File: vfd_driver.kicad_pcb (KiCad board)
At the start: 2 copper layers, 35 parts, among them CON1 AVR-ISP-6, J1 Conn_01x02, J2 futaba_7_lt_44z, J3 Input, Q1 IRLZ34, Q2 60N03L, Q3 BC817, Q4 BC807, Q5 BC817, Q6 BC807, T1 Transformer_1P_SS, U1 ATTINY13-20PU, U2 74HC595, U3 74HC595, U4 74HC595, U5 TBD62783A, U6 TBD62783A, U7 TBD62783A

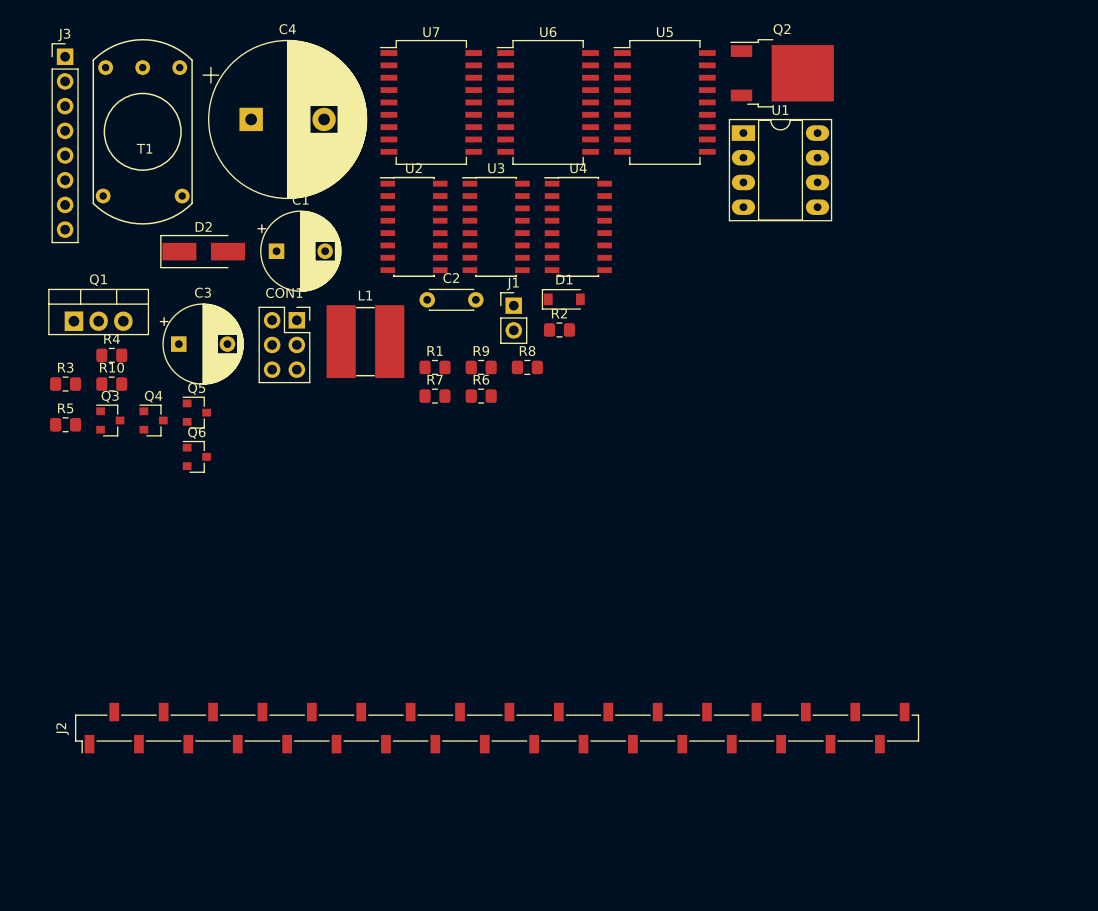
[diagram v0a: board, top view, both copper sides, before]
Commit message: add the datasheet of the vfd display
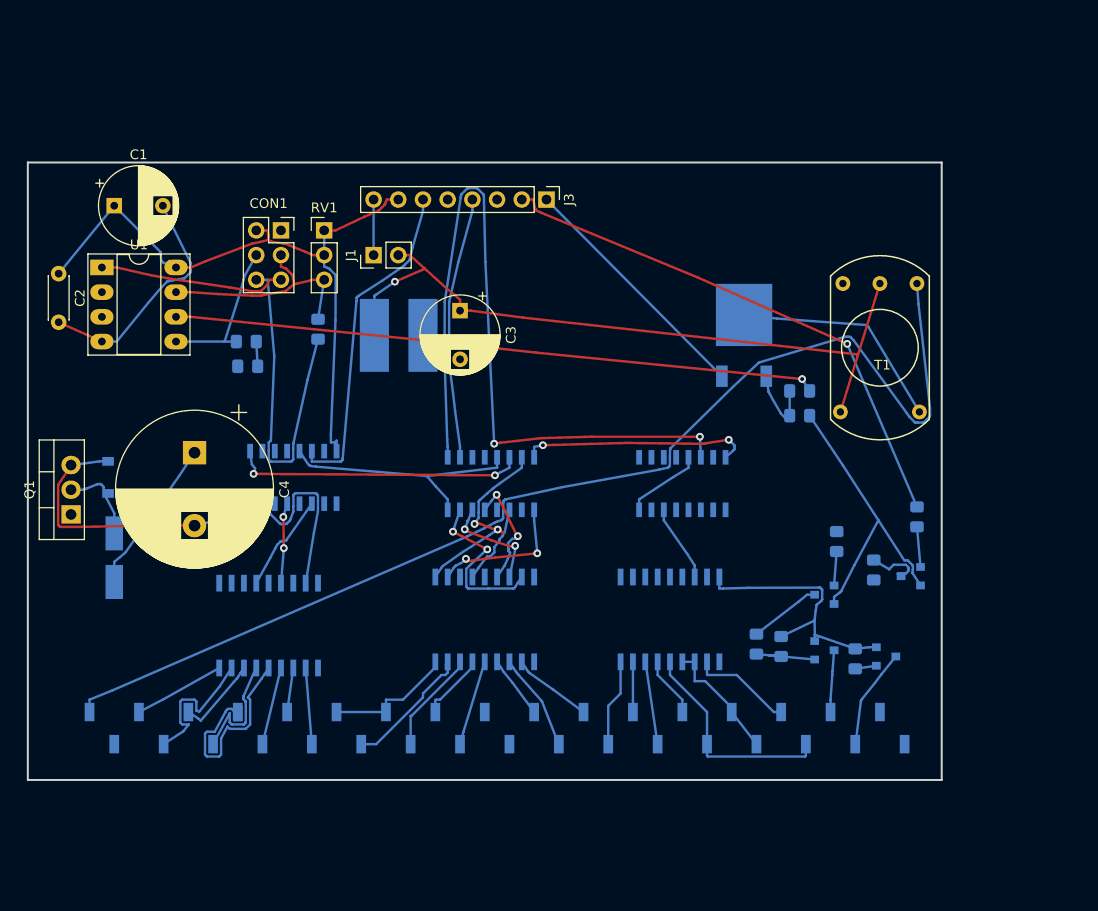
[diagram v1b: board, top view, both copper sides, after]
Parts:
- added R11: 1K, Resistor_SMD:R_0805_2012Metric_Pad1.15x1.40mm_HandSolder, B.Cu at (45.1, 29.8)
- added RV1: 10k, Connector_PinHeader_2.54mm:PinHeader_1x03_P2.54mm_Vertical, F.Cu at (45.7, 19.7)
- D1, D2, J2, L1, Q2, Q3, Q4, Q5, Q6, R1, R10, R2, R3, R4, R5, R6, R7, R8, R9, U2, U3, U4, U5, U6, U7: moved to B.Cu
- T1: footprint custom:Transformer_toroid_v_10mm -> modules:Transformer_toroid_v_10mm
- moved R5 88.1 mm to (106.7, 49.1), turned to 270 degrees
- moved Q3 83.9 mm to (106.0, 55.2), turned to 180 degrees
- moved Q4 79.1 mm to (103.5, 63.5)
- moved T1 79.0 mm to (102.9, 31.8)
- moved R3 75.5 mm to (94.6, 36.2)
- moved R10 71.5 mm to (90.2, 62.2), turned to 270 degrees
- moved R4 71.0 mm to (94.6, 38.7)
- moved Q6 67.5 mm to (97.2, 62.9)
- moved U5 67.5 mm to (40.0, 60.3), turned to 270 degrees
- moved U1 67.4 mm to (22.9, 23.5)
- moved Q5 67.2 mm to (97.2, 57.1), turned to 180 degrees
- moved U7 58.6 mm to (81.3, 59.7), turned to 270 degrees
- moved U6 53.6 mm to (62.2, 59.7), turned to 270 degrees
- moved J3 51.6 mm to (68.6, 16.5), turned to 270 degrees
- moved D1 50.4 mm to (23.5, 45.1), turned to 90 degrees
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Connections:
- net /SCK renamed /ADC
- J2 pad 17: (no net) -> Net-(J2-Pad17)
- J2 pad 18: (no net) -> Net-(J2-Pad18)
- J2 pad 2: (no net) -> Net-(J2-Pad2)
- J2 pad 33: (no net) -> Net-(J2-Pad33)
- U1 pad 2: (no net) -> Net-(U1-Pad2)
- U1 pad 3: (no net) -> Net-(U1-Pad3)
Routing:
- net GND: track 0.00 -> 182.6 mm
- net /FIL_n: track 0.00 -> 117.9 mm
- net VCC: track 0.00 -> 93.2 mm, vias 0 -> 2
- net /Q1: track 0.00 -> 79.0 mm, vias 0 -> 2
- net /5VOLT: track 0.00 -> 74.2 mm, vias 0 -> 1
- net /FILAMENT: track 0.00 -> 66.2 mm, vias 0 -> 1
- net /GRAD: track 0.00 -> 55.4 mm, vias 0 -> 1
- net +36V: track 0.00 -> 43.8 mm
- net /DATA: track 0.00 -> 34.1 mm
- net /Q0: track 0.00 -> 30.1 mm, vias 0 -> 2
- net /nSRCLR: track 0.00 -> 26.9 mm
- net /S6: track 0.00 -> 24.4 mm
- net /ADC: track 0.00 -> 23.3 mm
- net Net-(Q2-Pad2): track 0.00 -> 23.1 mm
- net /G1: track 0.00 -> 22.7 mm
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- added copper zone on B.Cu, net GND
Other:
- board outline added: 94 x 63.5 mm
- net class power added: clearance 0.2, trace_width 0.508, via_dia 0.8, via_drill 0.4
- net class signal added: clearance 0.2, trace_width 0.4064, via_dia 0.8, via_drill 0.4

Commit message: working on layout
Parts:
- added R12: 0, Resistor_SMD:R_1206_3216Metric, B.Cu at (31.0, 40.6)
- moved L1 33.9 mm to (23.4, 46.3), turned to 270 degrees
- moved R11 23.9 mm to (21.7, 34.7), turned to 0 degrees
- moved C4 17.8 mm to (31.2, 60.3), turned to 90 degrees
- moved J1 11.5 mm to (43.2, 30.9), turned to 0 degrees
- moved D1 11.1 mm to (17.8, 54.6)
- moved D2 10.7 mm to (21.2, 63.6), turned to 180 degrees
- moved Q1 9.44 mm to (20.6, 58.3)
- moved RV1 9.16 mm to (36.6, 20.2)
- moved R2 8.75 mm to (30.0, 37.5)
- moved R1 8.57 mm to (30.0, 34.8)
- moved C3 6.50 mm to (53.2, 28.4), turned to 180 degrees
- moved CON1 5.34 mm to (41.5, 25.0), turned to 180 degrees
- moved U2 1.20 mm to (41.5, 45.7)
- moved U5 1.14 mm to (40.0, 59.2)
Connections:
- C3 pad 1: /5VOLT -> +5V
- J3 pad 3: /RCLK -> /DATA
- J3 pad 4: /nSRCLR -> /RCLK
- J3 pad 6: /DATA -> /nSRCLR
- L1 pad 1: /5VOLT -> Net-(L1-Pad1)
- U2 pad 1: Net-(U2-Pad1) -> /Q1B
- U2 pad 15: Net-(U2-Pad15) -> /Q1A
- U2 pad 2: Net-(U2-Pad2) -> /Q1C
- U2 pad 3: Net-(U2-Pad3) -> /Q1D
- U2 pad 4: Net-(U2-Pad4) -> /Q1E
- U2 pad 5: Net-(U2-Pad5) -> /Q1F
- U2 pad 6: Net-(U2-Pad6) -> /Q1G
- U2 pad 7: Net-(U2-Pad7) -> /Q1H
- U3 pad 1: Net-(U3-Pad1) -> /Q2B
- U3 pad 15: Net-(U3-Pad15) -> /Q2A
- U3 pad 2: Net-(U3-Pad2) -> /Q2C
- U3 pad 3: Net-(U3-Pad3) -> /Q2D
- U3 pad 4: Net-(U3-Pad4) -> /Q2E
- U3 pad 5: Net-(U3-Pad5) -> /Q2F
- U3 pad 6: Net-(U3-Pad6) -> /Q2G
- U3 pad 7: Net-(U3-Pad7) -> /Q2H
- U4 pad 1: Net-(U4-Pad1) -> /Q3B
- U4 pad 15: Net-(U4-Pad15) -> /Q3A
- U4 pad 2: Net-(U4-Pad2) -> /Q3C
- U4 pad 3: Net-(U4-Pad3) -> /Q3D
- U4 pad 4: Net-(U4-Pad4) -> /Q3E
- U4 pad 5: Net-(U4-Pad5) -> /Q3F
- U4 pad 6: Net-(U4-Pad6) -> /Q3G
- U4 pad 7: Net-(U4-Pad7) -> /Q3H
- U5 pad 1: Net-(U2-Pad15) -> /Q1H
- U5 pad 2: Net-(U2-Pad1) -> /Q1G
- U5 pad 3: Net-(U2-Pad2) -> /Q1F
- U5 pad 4: Net-(U2-Pad3) -> /Q1E
- U5 pad 5: Net-(U2-Pad4) -> /Q1D
- U5 pad 6: Net-(U2-Pad5) -> /Q1C
- U5 pad 7: Net-(U2-Pad6) -> /Q1B
- U5 pad 8: Net-(U2-Pad7) -> /Q1A
- U6 pad 1: Net-(U3-Pad15) -> /Q2H
- U6 pad 2: Net-(U3-Pad1) -> /Q2G
- U6 pad 3: Net-(U3-Pad2) -> /Q2F
- U6 pad 4: Net-(U3-Pad3) -> /Q2E
- U6 pad 5: Net-(U3-Pad4) -> /Q2D
- U6 pad 6: Net-(U3-Pad5) -> /Q2C
- U6 pad 7: Net-(U3-Pad6) -> /Q2B
- U6 pad 8: Net-(U3-Pad7) -> /Q2A
- U7 pad 1: Net-(U4-Pad15) -> /Q3H
- U7 pad 2: Net-(U4-Pad1) -> /Q3G
- U7 pad 3: Net-(U4-Pad2) -> /Q3F
- U7 pad 4: Net-(U4-Pad3) -> /Q3E
- U7 pad 5: Net-(U4-Pad4) -> /Q3D
- U7 pad 6: Net-(U4-Pad5) -> /Q3C
- U7 pad 7: Net-(U4-Pad6) -> /Q3B
- U7 pad 8: Net-(U4-Pad7) -> /Q3A
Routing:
- net GND: track 182.6 -> 30.6 mm, vias 0 -> 2
- net /FIL_n: track 117.9 -> 0.00 mm
- net /SRCLK: track 0.00 -> 83.7 mm, vias 0 -> 4
- net /RCLK: track 0.00 -> 82.2 mm, vias 0 -> 4
- net +36V: track 43.8 -> 109.8 mm
- net /5VOLT: track 74.2 -> 14.4 mm, vias 1 -> 0
- net /nSRCLR: track 26.9 -> 84.1 mm, vias 0 -> 2
- net /GRAD: track 55.4 -> 0.00 mm, vias 1 -> 0
- net /FILAMENT: track 66.2 -> 12.9 mm, vias 1 -> 0
- net VCC: track 93.2 -> 140.1 mm, vias 2 -> 4
- net /Q1: track 79.0 -> 33.3 mm
- net Net-(Q1-Pad1): track 2.54 -> 30.2 mm
- net +5V: track 5.71 -> 30.0 mm
- net Net-(Q2-Pad2): track 23.1 -> 0.00 mm
- net Net-(U3-Pad15): track 21.1 -> 0.00 mm, vias 2 -> 0
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
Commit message: zwischenschritt
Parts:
- added R13: 0, Resistor_SMD:R_1206_3216Metric, B.Cu at (35.7, 35.6)
- added R14: 0, Resistor_SMD:R_1206_3216Metric, B.Cu at (70.6, 52.8)
- moved R8 29.1 mm to (70.6, 60.3)
- moved R5 15.2 mm to (91.8, 46.1)
- moved Q3 12.6 mm to (95.5, 48.3)
- moved R4 11.6 mm to (87.9, 29.3), turned to 270 degrees
- moved R3 11.4 mm to (85.5, 29.3), turned to 270 degrees
- moved Q2 11.0 mm to (85.6, 19.9)
- moved R6 10.2 mm to (97.9, 53.8)
- moved Q4 10.0 mm to (101.3, 53.7)
- moved Q6 9.49 mm to (94.6, 53.7)
- moved R9 8.89 mm to (91.2, 53.7)
- moved T1 8.08 mm to (97.0, 26.2), turned to 180 degrees
- moved Q5 7.05 mm to (90.7, 59.9)
- moved R7 5.19 mm to (100.3, 59.4), turned to 180 degrees
- moved R10 4.95 mm to (93.9, 58.9), turned to 90 degrees
- moved C3 4.36 mm to (53.8, 24.1)
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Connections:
- J2 pad 17: Net-(J2-Pad17) -> (no net)
- J2 pad 18: Net-(J2-Pad18) -> (no net)
- J2 pad 2: Net-(J2-Pad2) -> (no net)
- J2 pad 28: /b -> /a
- J2 pad 33: Net-(J2-Pad33) -> (no net)
- U1 pad 2: Net-(U1-Pad2) -> (no net)
- U1 pad 3: Net-(U1-Pad3) -> (no net)
- U6 pad 12: /G3 -> /g
- U6 pad 13: /g -> /G3
- U7 pad 13: /b -> /a
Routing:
- net /FIL_n: track 0.00 -> 137.2 mm, vias 0 -> 2
- net /5VOLT: track 14.4 -> 94.4 mm, vias 0 -> 2
- net /FIL_p: track 0.00 -> 50.9 mm
- net /FILAMENT: track 12.9 -> 61.1 mm, vias 0 -> 2
- net /GRAD: track 0.00 -> 46.9 mm
- net /Q2: track 0.00 -> 26.0 mm
- net GND: track 30.6 -> 50.5 mm
- net Net-(Q5-Pad1): track 3.51 -> 22.3 mm
- net /Q1: track 33.3 -> 49.6 mm
- net Net-(Q3-Pad3): track 6.17 -> 20.9 mm
- net /S11: track 6.36 -> 20.2 mm
- net /a: track 0.00 -> 12.7 mm
- net Net-(Q2-Pad2): track 0.00 -> 10.9 mm
- net /SRCLK: track 83.7 -> 93.7 mm
- net +5V: track 30.0 -> 20.2 mm
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
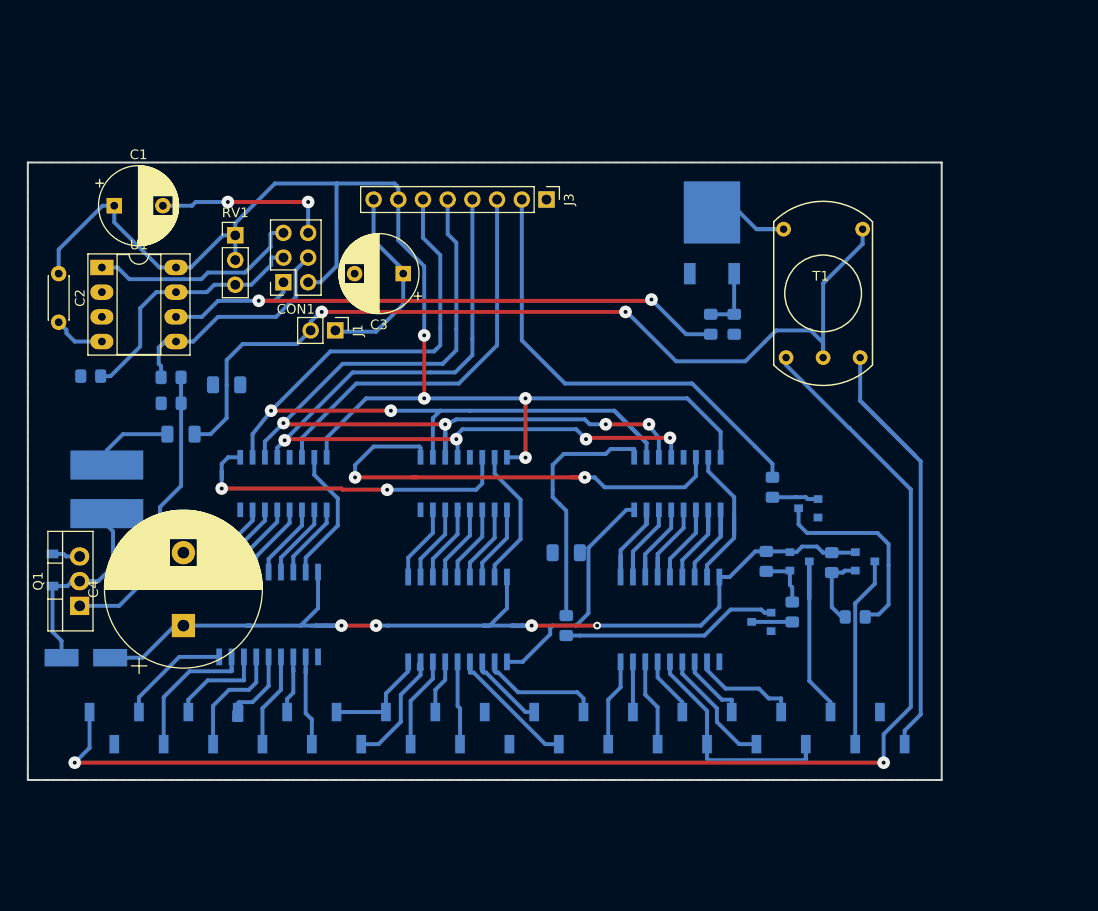
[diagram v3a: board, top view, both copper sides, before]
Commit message: remove the ISP connector
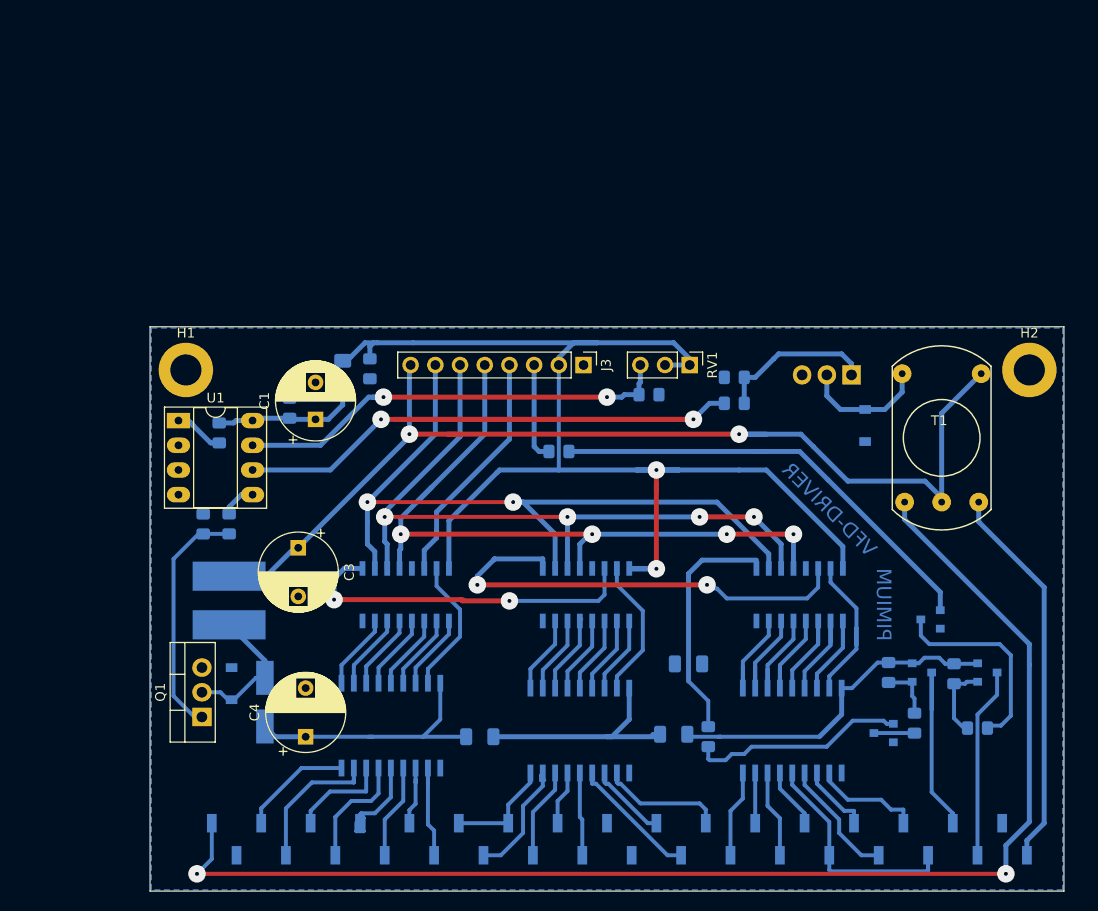
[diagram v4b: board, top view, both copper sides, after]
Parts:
- removed CON1: AVR-ISP-6, Connector_PinSocket_2.54mm:PinSocket_2x03_P2.54mm_Vertical
- removed J1: Conn_01x02, Connector_PinHeader_2.54mm:PinHeader_1x02_P2.54mm_Vertical
- added C5: 10n, Capacitor_SMD:C_0805_2012Metric_Pad1.15x1.40mm_HandSolder, B.Cu at (50.4, 33.9)
- added D3: SD_103BW, Diode_SMD:D_SOD-123, B.Cu at (101.3, 39.8)
- added H1: MH, MountingHole:MountingHole_3.2mm_M3_DIN965_Pad, F.Cu at (31.5, 34.0)
- added H2: MH, MountingHole:MountingHole_3.2mm_M3_DIN965_Pad, F.Cu at (118.2, 34.0)
- added L2: 33, Inductor_SMD:L_1206_3216Metric_Pad1.42x1.75mm_HandSolder, B.Cu at (47.6, 34.6)
- added R15: 10k, Resistor_SMD:R_0805_2012Metric_Pad1.15x1.40mm_HandSolder, B.Cu at (34.9, 40.5)
- C1: value 470u -> 10u; footprint Capacitor_THT:CP_Radial_D8.0mm_P5.00mm -> Capacitor_THT:CP_Radial_D8.0mm_P3.80mm
- C2: footprint Capacitor_THT:C_Disc_D4.3mm_W1.9mm_P5.00mm -> Capacitor_SMD:C_0805_2012Metric_Pad1.15x1.40mm_HandSolder; moved to B.Cu
- C3: value 220u -> 10u/63v
- C4: value 220u/50V -> 10u/63v; footprint Capacitor_THT:CP_Radial_D16.0mm_P7.50mm -> Capacitor_THT:CP_Radial_D8.0mm_P5.00mm
- Q2: value 60N03L -> IRF640; footprint Package_TO_SOT_SMD:TO-252-2 -> Package_TO_SOT_THT:TO-220-3_Vertical
- T1: footprint modules:Transformer_toroid_v_10mm -> custom_footprint:Transformer_toroid_v_18mm
- moved R13 58.4 mm to (81.7, 71.5)
- moved R11 57.4 mm to (79.1, 36.6), turned to 180 degrees
- moved RV1 48.6 mm to (83.3, 33.5), turned to 270 degrees
- moved R12 43.7 mm to (61.7, 71.8), turned to 0 degrees
- moved C3 30.2 mm to (43.1, 52.3), turned to 270 degrees
- moved C1 30.2 mm to (44.8, 39.1), turned to 90 degrees
- moved C2 27.5 mm to (42.2, 38.0), turned to 90 degrees
- moved R5 22.3 mm to (69.9, 42.4), turned to 0 degrees
- moved D1 21.8 mm to (36.2, 66.3)
- moved Q2 20.5 mm to (99.9, 34.5), turned to 180 degrees
- moved T1 19.2 mm to (109.2, 41.0)
- moved D2 19.0 mm to (39.6, 68.2), turned to 90 degrees
- moved R8 18.5 mm to (85.2, 71.7)
- moved U1 17.6 mm to (30.7, 39.2)
- moved J3 17.4 mm to (72.4, 33.5)
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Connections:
- C1 pad 1: VCC -> VDD
- C2 pad 1: VCC -> VDD
- J3 pad 2: /GRAD -> VCC
- J3 pad 3: /DATA -> /GRAD
- J3 pad 4: /RCLK -> /DATA
- J3 pad 5: /SRCLK -> /RCLK
- J3 pad 6: /nSRCLR -> /SRCLK
- J3 pad 7: VCC -> /nSRCLR
- L1 pad 1: Net-(L1-Pad1) -> +5V
- R12 pad 1: /5VOLT -> +36V
- R12 pad 2: Net-(L1-Pad1) -> +36V
- R13 pad 1: GND -> +36V
- R13 pad 2: GND -> +36V
- T1 pad 1: /5VOLT -> +5V
- T1 pad 4: /5VOLT -> +5V
- U1 pad 8: VCC -> VDD
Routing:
- net /5VOLT: track 94.4 -> 0.00 mm, vias 2 -> 0
- net +5V: track 20.2 -> 108.8 mm, vias 0 -> 2
- net GND: track 50.5 -> 0.00 mm, vias 2 -> 0
- net Net-(Q3-Pad1): track 4.77 -> 46.9 mm
- net /GRAD: track 46.9 -> 10.1 mm
- net /HIGH_VOLT: track 26.1 -> 3.65 mm
- net /FILAMENT: track 61.1 -> 81.7 mm
- net /Q0: track 35.3 -> 55.7 mm
- net /ADC: track 26.6 -> 46.5 mm, vias 0 -> 2
- net /SRCLK: track 93.7 -> 75.1 mm
- net /DATA: track 42.4 -> 25.9 mm
- net /RST: track 21.9 -> 5.68 mm
- net VDD: track 0.00 -> 15.1 mm
- net /nSRCLR: track 92.6 -> 78.4 mm
- net /FIL_p: track 50.9 -> 39.8 mm
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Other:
- board size 94 x 63.5 mm -> 94 x 58 mm
- board text added: "PIMIUM"
- board text added: "VFD-DRIVER"
